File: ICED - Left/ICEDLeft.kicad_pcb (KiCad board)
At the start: 2 copper layers, 175.4 x 145 mm, 164 parts, among them P1 FLASH_HDR, P2 USBC, P3 CONN_17, P4 USB3_AFEMALE, Q1 TC1264, U1 MK20DX256VLH7, U2 IS31FL3731C, X1 CRYSTAL

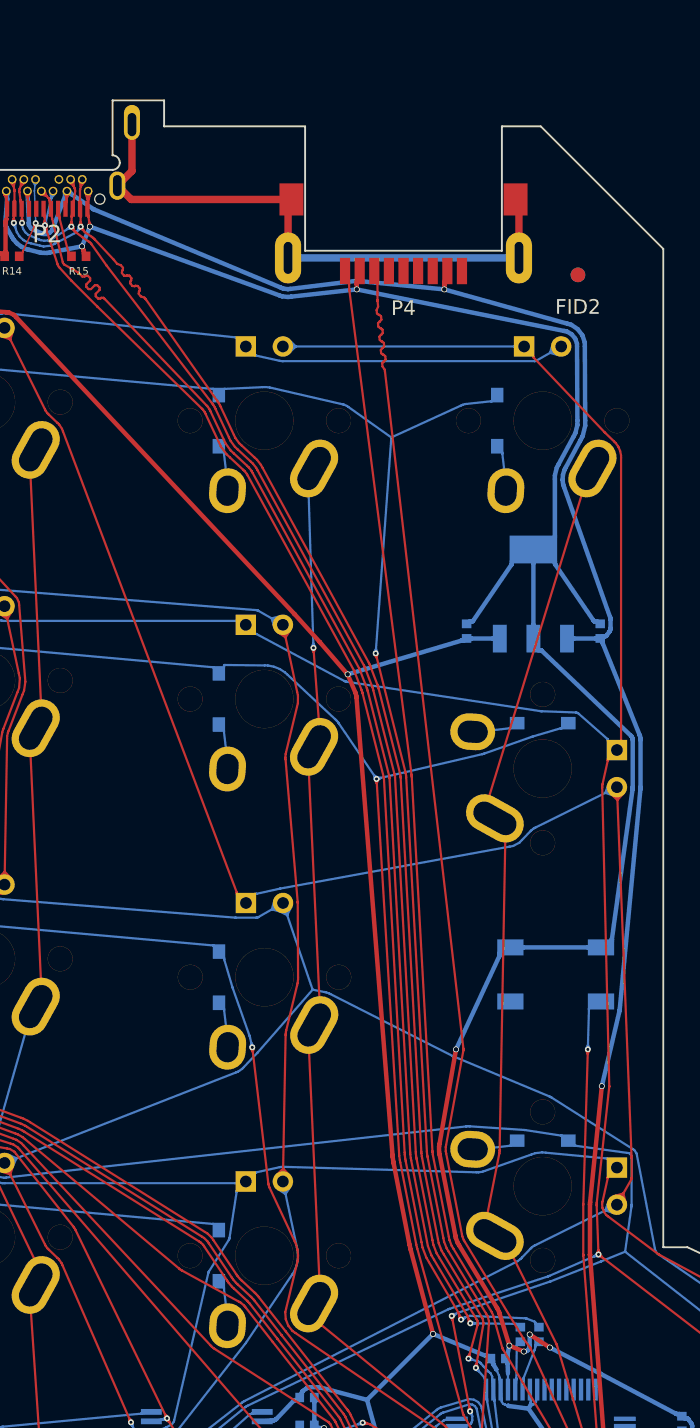
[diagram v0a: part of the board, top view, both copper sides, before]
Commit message: Update USB A connector
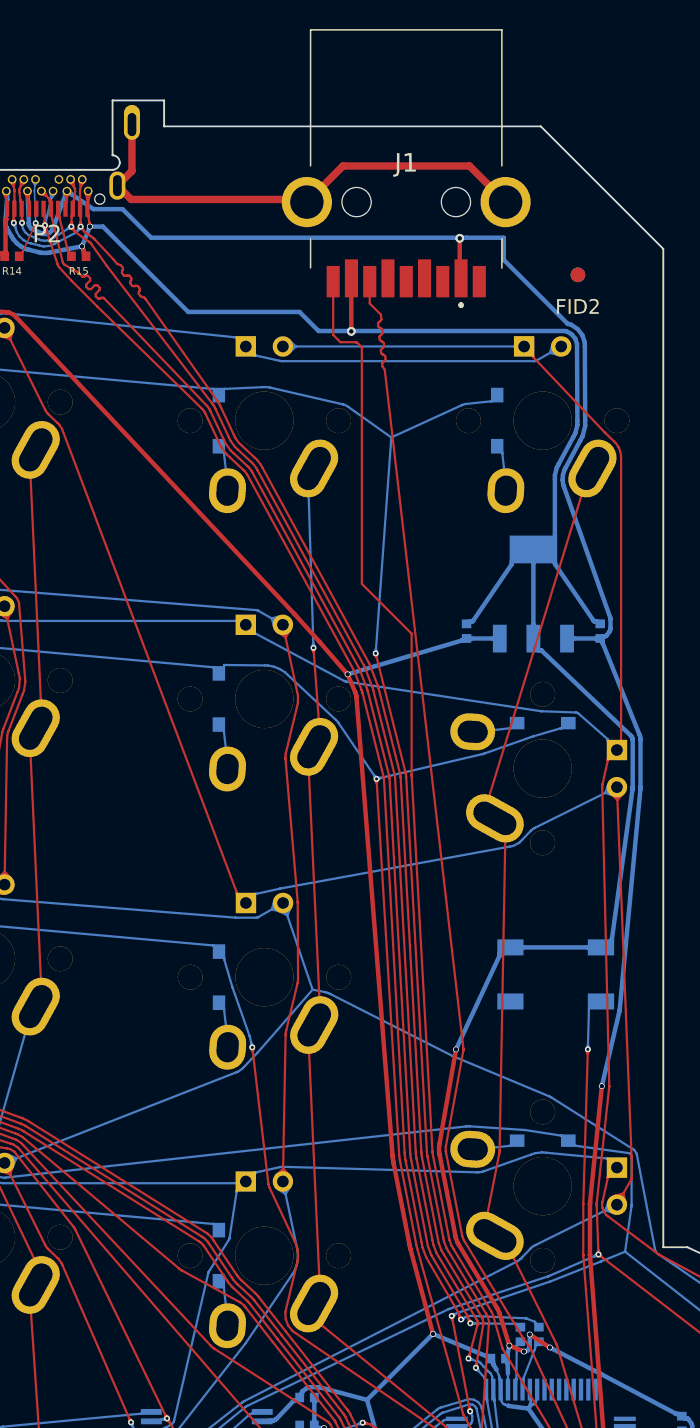
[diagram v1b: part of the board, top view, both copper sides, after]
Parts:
- removed IC_LOGO: , prettylib:IC_LOGO
- removed P4: USB3_AFEMALE, prettylib:USB3_AFEMALE_MOD
- added G***: LOGO, prettylib:dickbut, B.Cu at (33.3, 31.9)
- added J1: 692122030100, prettylib:692122030100, F.Cu at (135.6, 32.7)
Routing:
- net /GND: track 45.5 -> 38.4 mm
- net VSS: track 399.5 -> 403.7 mm
- net +5V: track 218.9 -> 223.0 mm
- net /mcu/TX0: track 177.4 -> 179.3 mm
- net /mcu/RX0: track 171.1 -> 170.5 mm
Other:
- outline, holes or cut-outs redrawn
- board text added: "ICED-L Rev 1.3 Batch 01"
- board text removed: "ICED-L Rev 1.2b Batch __"
